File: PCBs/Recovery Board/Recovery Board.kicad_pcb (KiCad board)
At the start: 2 copper layers, 85 x 56 mm, 35 parts, among them J1 Conn_01x02, J2 Conn_01x02, J3 Conn_01x02, J4 Conn_01x02, J5 Conn_01x02, J6 Conn_01x02, J7 Conn_01x02, U1 R-78E3.3-0.5, U2 PI4ULS5V201TAEX-RESCUE-instru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, U3 PI4ULS5V201TAEX-RESCUE-instru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

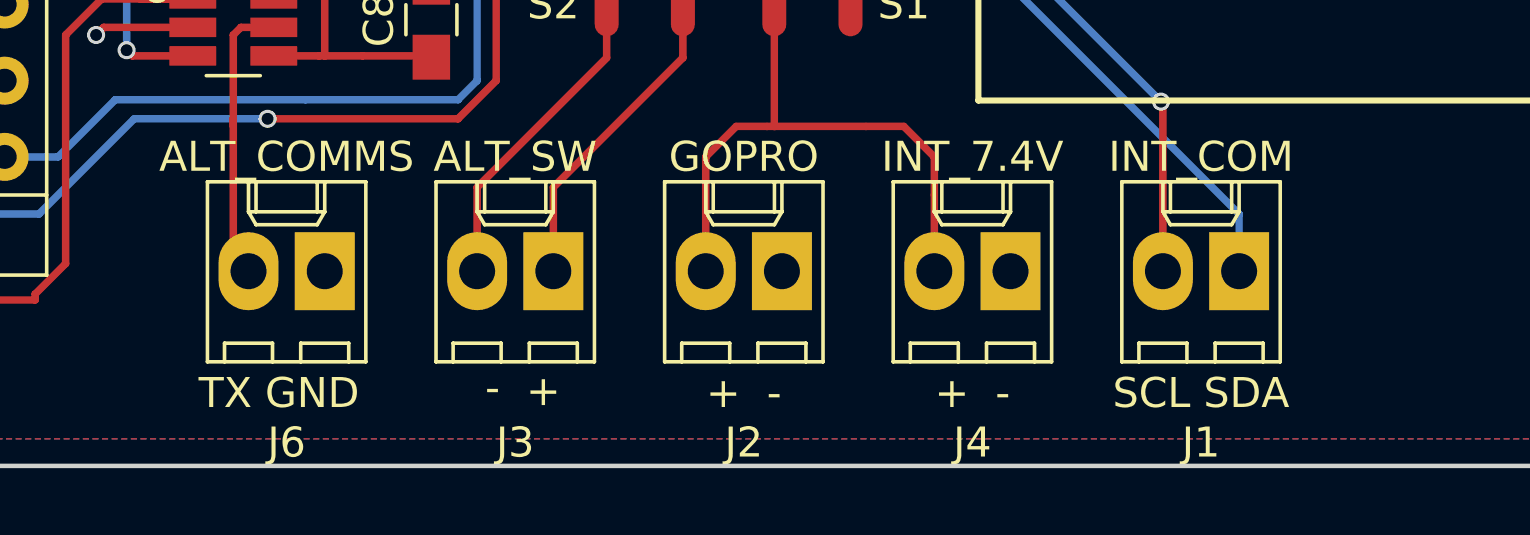
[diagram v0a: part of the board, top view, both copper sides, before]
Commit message: Connector Changes
Flipped the transponder jst-ph connectors
Replaced the molex footprint on recovery with the correct one
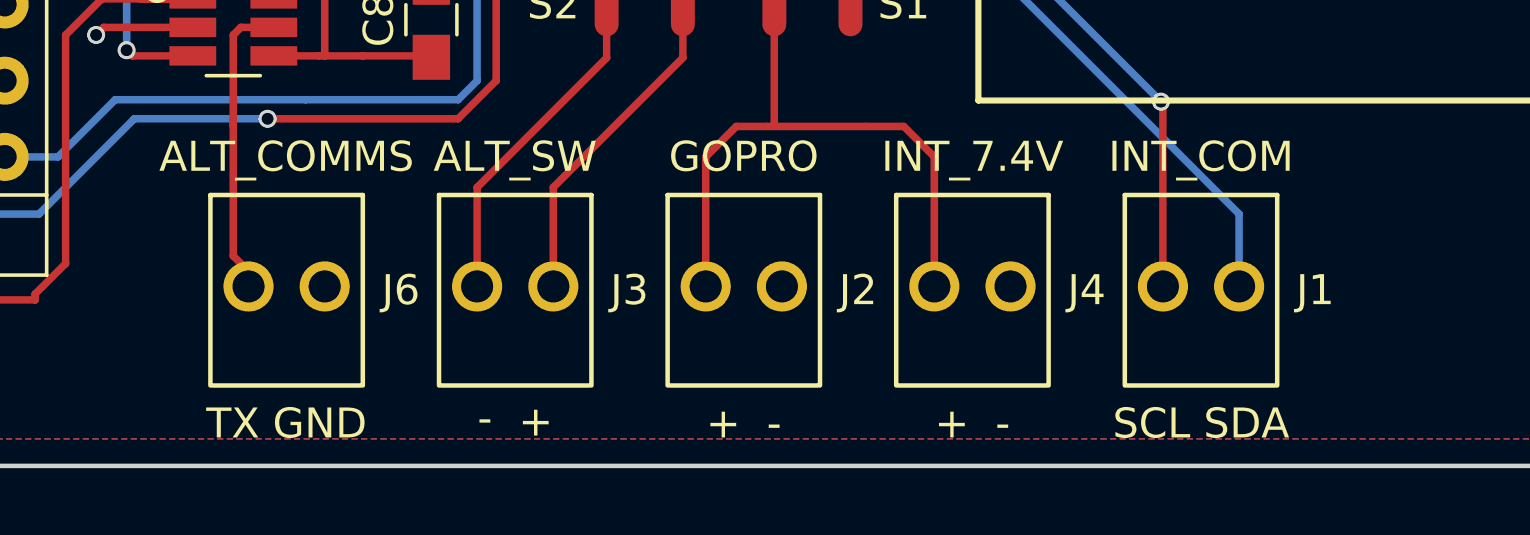
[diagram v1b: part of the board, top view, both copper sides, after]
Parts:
- J1, J2, J3, J4, J6: footprint Connectors_Molex:Molex_KK-6410-02_02x2.54mm_Straight -> molex:molex_kk_22-23-2021
- moved J1 2.84 mm to (148.6, 141.0)
- moved J2 2.84 mm to (133.3, 141.0)
- moved J4 2.84 mm to (141.0, 141.0)
- moved J3 2.84 mm to (125.7, 141.0)
- moved J6 2.84 mm to (118.1, 141.0)

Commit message: Changes to recovery board to fix found issues
Swapped pin 1 & 2 on the CPC1002N relays
Removed the screen from the back of the xbee pins
Added an indicator for the install direction for arduino
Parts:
- turned S1 to 180 degrees
- turned S2 to 180 degrees
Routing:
- net Net-(R5-Pad1): track 11.1 -> 14.8 mm
- net Net-(R6-Pad1): track 15.8 -> 18.7 mm
